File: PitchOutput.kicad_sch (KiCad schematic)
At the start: 25 parts, among them J3 Pitch, J8 CC, U3 TL072, U4 TL072

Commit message: add gerbers and bom
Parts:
- C10, C11, C12, C13, C14, C7: LCSC (none) -> C1588
- J3, J8, JP1, RV1, RV2: JLCPCB_IGNORE (none) -> 1
- R10, R23, R7: LCSC (none) -> C21190
- R12, R13, R14, R15, R16, R17: LCSC (none) -> C22809
- R25, R4: LCSC (none) -> C25803
- R3: LCSC (none) -> C22935
- U3, U4: LCSC (none) -> C6961; LCSC PN C6961 -> (none)

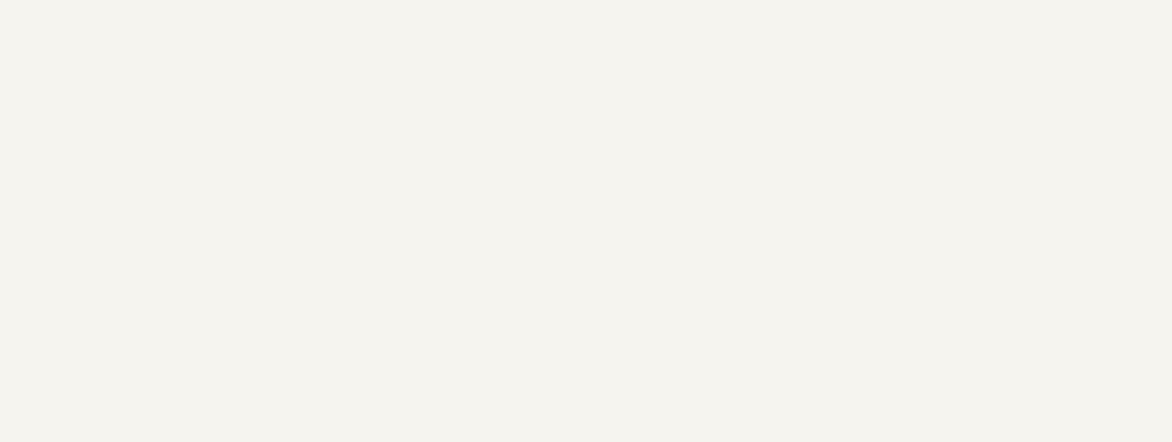
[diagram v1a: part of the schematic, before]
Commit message: add rev 2 and rev 3, now with correct trs midi A
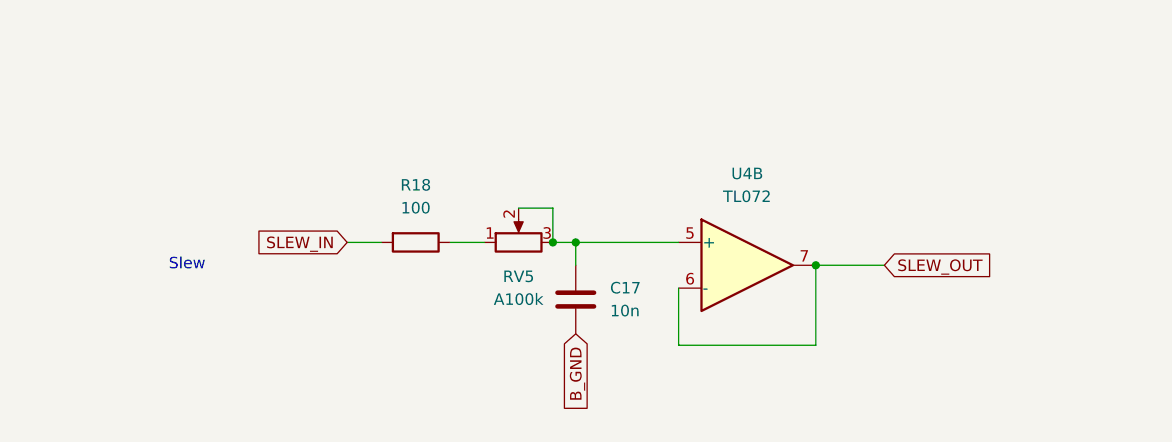
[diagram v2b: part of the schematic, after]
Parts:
- added C17: 10n, Capacitor_SMD:C_0603_1608Metric, symbol Device:C
- added R18: 100, Resistor_SMD:R_0603_1608Metric, symbol Device:R
- added RV5: A100k, EuroRackTools:Potentiometer_Alpha_RD901F-40-00D_Single_Vertical, symbol Device:R_Potentiometer
- added unit 2 of U4
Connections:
- net B_GND: now also C17.2
- net SLEW_IN: now also R18.2
- net SLEW_OUT: now also U4.6 (-), U4.7
- new net: C17.1, RV5.2, RV5.3, U4.5 (+)
- new net: R18.1, RV5.1
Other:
- note added: "Slew"
